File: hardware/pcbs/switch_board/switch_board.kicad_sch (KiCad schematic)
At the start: 68 parts, among them J6 I/O, J8 UART, U1 RTL8367S, U2 TPS562231, U3 TPS562231, U4 W25Q32JVSS, U5 24LC64, Y1 TSX-3225

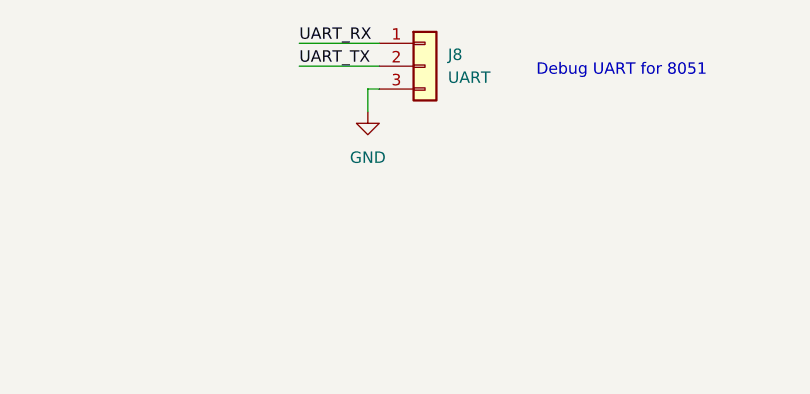
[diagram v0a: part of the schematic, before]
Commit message: switch_board: add additional power connector
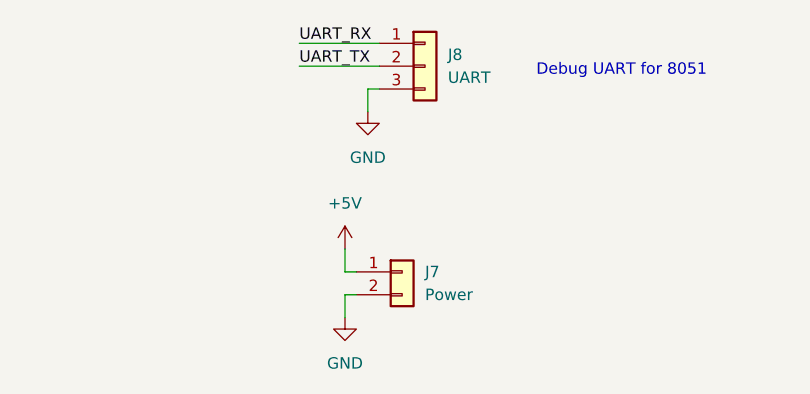
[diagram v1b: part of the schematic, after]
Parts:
- added J7: Power, Library:mta100_01x2_P2.54_647050-2, symbol Connector_Generic:Conn_01x02
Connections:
- net +5V: now also J7.1 (Pin_1)
- net GND: now also J7.2 (Pin_2)

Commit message: pcbs: update purchase info
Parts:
- C1, C2: Part (none) -> C 27pF 16V 0603; Shop (none) -> https://store.comet.bg/Catalogue/Product/5610/
- C10, C11, C20, C28, C3, C34, C4, C5, C6, C7, C8, C9: Part (none) -> C 100nF 16V 0603; Shop (none) -> https://store.comet.bg/Catalogue/Product/38000/
- C12, C13, C21, C24: Part (none) -> C 10μF 10V 0603; Shop (none) -> https://store.comet.bg/Catalogue/Product/43703/
- C19, C22, C23, C25, C26, C27: Part (none) -> C 22μF 6.3V 0603; Shop (none) -> https://store.comet.bg/Catalogue/Product/50230/
- J6: Part (none) -> 640454-6; Shop (none) -> https://eu.mouser.com/ProductDetail/TE-Connectivity/640454-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
- J7: Part (none) -> 640454-2; Shop (none) -> https://eu.mouser.com/ProductDetail/TE-Connectivity/640454-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
- J8, TP1, TP2, TP3: now left out of the parts list
- L1, L2: Part (none) -> BWVF005050201R5T00; Shop (none) -> https://eu.mouser.com/ProductDetail/Pulse-Electronics/BWVF0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
- R11, R14, R26, R27, R32, R37, R38, R39, R40, R42, R44, R45, R46, R48: Part (none) -> R 4.7kΩ 125mW 1% 0603; Shop (none) -> https://store.comet.bg/Catalogue/Product/4411/
- R12, R49: Part (none) -> R 1kΩ 125mW 1% 0603; Shop (none) -> https://store.comet.bg/Catalogue/Product/4405/
- R13: Part (none) -> R 2.49kΩ 125mW 1% 0402; Shop (none) -> https://www.tme.eu/lv/en/details/rc0402fr-072k49l/smd-resis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
- R15: Part (none) -> R 6.2kΩ 125mW 1% 0603; Shop (none) -> https://store.comet.bg/Catalogue/Product/9992/
- R16: Part (none) -> R 3.3kΩ 125mW 1% 0603; Shop (none) -> https://store.comet.bg/Catalogue/Product/9936/
- R2: Part (none) -> R 4.99kΩ 125mW 1% 0603; Shop (none) -> https://store.comet.bg/Catalogue/Product/35342/
- R3, R9: Part (none) -> R 10kΩ 125mW 1% 0603; Shop (none) -> https://store.comet.bg/Catalogue/Product/4415/
- R8: Part (none) -> R 39kΩ 125mW 1% 0603; Shop (none) -> https://store.comet.bg/Catalogue/Product/4781/
- U1: Part (none) -> RTL8367S; Shop (none) -> https://www.lcsc.com/product-detail/C2760849.html
- U2, U3: Part (none) -> TPS562231DRLR; Shop (none) -> https://www.mouser.bg/ProductDetail/Texas-Instruments/TPS56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
- Y1: Part (none) -> X322525MOB4SI; Shop (none) -> https://www.lcsc.com/product-detail/Crystals_YXC-Crystal-Os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

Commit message: switch_board: allow another inductor
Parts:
- L1, L2: Part BWVF005050201R5T00 -> BWVF005050201R5T00 or 74404054015
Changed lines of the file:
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@@
 			)
 		)
-		(property "Part" "BWVF005050201R5T00"
+		(property "Part" "BWVF005050201R5T00 or 74404054015"
 			(at 250.19 158.75 0)
 			(effects
@@
 			)
 		)
-		(property "Part" "BWVF005050201R5T00"
+		(property "Part" "BWVF005050201R5T00 or 74404054015"
 			(at 250.19 102.87 0)
 			(effects

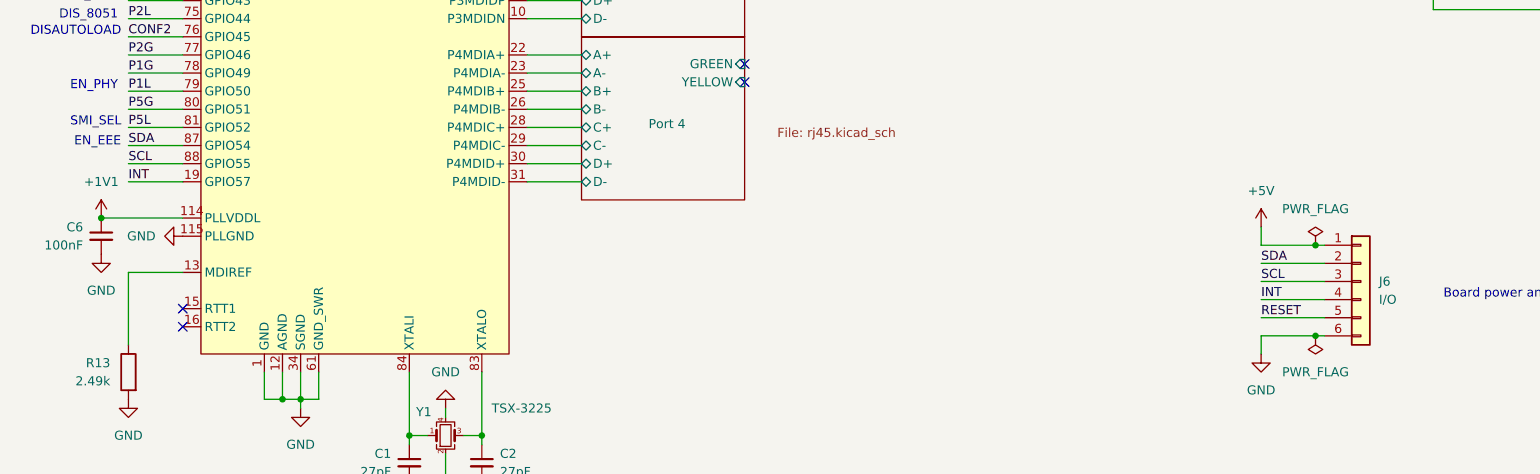
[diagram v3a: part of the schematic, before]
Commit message: boards: fix many silly bugs discovered during testing
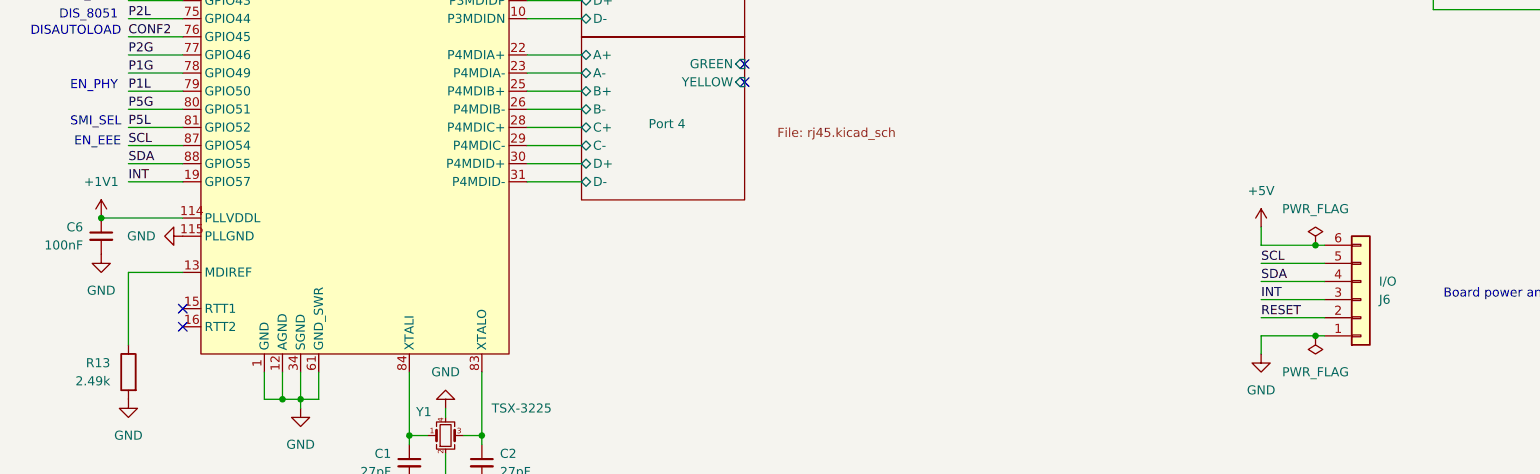
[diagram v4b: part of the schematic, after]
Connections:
- net +5V: now also J6.6 (Pin_6); no longer J6.1 (Pin_1)
- net GND: now also J6.1 (Pin_1); no longer J6.6 (Pin_6)
- net INT: now also J6.3 (Pin_3); no longer J6.4 (Pin_4)
- net RESET: now also J6.2 (Pin_2); no longer J6.5 (Pin_5)
- net SCL: now also J6.5 (Pin_5), U1.87 (GPIO54); no longer J6.3 (Pin_3), U1.88 (GPIO55)
- net SDA: now also J6.4 (Pin_4), U1.88 (GPIO55); no longer J6.2 (Pin_2), U1.87 (GPIO54)
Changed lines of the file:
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@@
 	)
 	(label "SCL"
-		(at 212.09 217.17 0)
+		(at 212.09 214.63 0)
 		(fields_autoplaced yes)
 		(effects
@@
 	)
 	(label "SDA"
-		(at 53.34 198.12 0)
+		(at 53.34 200.66 0)
 		(fields_autoplaced yes)
 		(effects
@@
 	)
 	(label "SDA"
-		(at 212.09 214.63 0)
+		(at 212.09 217.17 0)
 		(fields_autoplaced yes)
 		(effects
@@
 	)
 	(label "SCL"
-		(at 53.34 200.66 0)
+		(at 53.34 198.12 0)
 		(fields_autoplaced yes)
 		(effects
@@
 	(symbol
 		(lib_id "Connector_Generic:Conn_01x06")
-		(at 226.06 217.17 0)
+		(at 226.06 219.71 0)
+		(mirror x)
 		(unit 1)
 		(exclude_from_sim no)
@@
 		(on_board yes)
 		(dnp no)
-		(fields_autoplaced yes)
 		(property "Reference" "J6"
-			(at 228.6 217.1699 0)
+			(at 228.6 219.7101 0)
 			(effects
 				(font
@@
 		)
 		(property "Value" "I/O"
-			(at 228.6 219.7099 0)
+			(at 228.6 217.1701 0)
 			(effects
 				(font
@@
 		)
 		(property "Footprint" "Library:mta100_01x6_P2.54_647050-6"
-			(at 226.06 217.17 0)
+			(at 226.06 219.71 0)
 			(effects
 				(font
@@
 		)
 		(property "Datasheet" "~"
-			(at 226.06 217.17 0)
+			(at 226.06 219.71 0)
 			(effects
 				(font
@@
 		)
 		(property "Description" "Generic connector, single row, 01x06, script generated (kicad-library-utils/schlib/autogen/connector/)"
-			(at 226.06 217.17 0)
+			(at 226.06 219.71 0)
 			(effects
 				(font
@@
 		)
 		(property "Part" "640454-6"
-			(at 226.06 217.17 0)
+			(at 226.06 219.71 0)
 			(effects
 				(font
@@
 		)
 		(property "Shop" "https://eu.mouser.com/ProductDetail/TE-Connectivity/640454-6?qs=%2F35zJ5USjonV0oil6hzIeQ%3D%3D"
-			(at 226.06 217.17 0)
+			(at 226.06 219.71 0)
 			(effects
 				(font
@@
 		(on_board yes)
 		(dnp no)
-		(fields_autoplaced yes)
 		(property "Reference" "J7"
 			(at 226.06 271.7799 0)

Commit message: switch_board: update some parts
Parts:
- J6: LCSC (none) -> C593126
- J7: LCSC (none) -> C86501
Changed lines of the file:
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@@
+			)
+		)
+		(property "LCSC" "C593126"
+			(at 226.06 219.71 0)
+			(effects
+				(font
+					(size 1.27 1.27)
+				)
+				(hide yes)
 			)
 		)
@@
 			(at 223.52 271.78 0)
 			(effects
+				(font
+					(size 1.27 1.27)
+				)
+				(hide yes)
+			)
+		)
+		(property "LCSC" "C86501"
+			(at 223.52 271.78 0)
+			(effects

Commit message: boards: update mta100 part numbers
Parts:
- J6: LCSC C593126 -> C86506; Part 640454-6 -> 640456-6
- J7: LCSC C86501 -> C86502; Part 640454-2 -> 640456-2
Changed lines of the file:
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@@
 			)
 		)
-		(property "Part" "640454-6"
+		(property "Part" "640456-6"
 			(at 226.06 219.71 0)
 			(effects
@@
 			)
 		)
-		(property "LCSC" "C593126"
+		(property "LCSC" "C86506"
 			(at 226.06 219.71 0)
 			(effects
@@
 			)
 		)
-		(property "Part" "640454-2"
+		(property "Part" "640456-2"
 			(at 223.52 271.78 0)
 			(effects
@@
 			)
 		)
-		(property "LCSC" "C86501"
+		(property "LCSC" "C86502"
 			(at 223.52 271.78 0)
 			(effects
